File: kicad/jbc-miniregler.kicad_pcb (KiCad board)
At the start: 2 copper layers, 110 x 100 mm, 176 parts, among them J1 Makita Plus, J10 Makita Minus, J12 ActivEnergy B2-, J13 ActivEnergy B1-, J2 Makita Minus, J4 USB_B, J5 AVR ISP, J6 ActivEnergy B2+, J7 ActivEnergy B1+, J8 Makita Plus, Q1 KND3508A, Q2 2N7002, Q3 MMBT3904, Q4 MMBT3904, Q5 ZXMP10A13FTA, SW1 UP, SW2 DOWN, SW3 ENTER, SW4 BACK, SW5 Reset, SW6 Ein/Aus, U1 OLED-128x32-Module, U10 MAX3232, U11 YD3082EESA, U12 TL431, U2 74LVC1G125, U3 NST175, U4 CH340C, U5 ATmega328P-AU, U6 GS8332-SR, U7 PN7006A, U8 XL7005A, U9 XL7005A, X1 POWER, X2 COM, X3 Lötkolben, X4 GND-Öse, Y1 16MHz

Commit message: HTML-BOM aktualisiert
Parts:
- added Item5: Buchsenleiste 4P, htl_virtual:Virtual-Item, F.Cu at (141.2, 151.6)
- added R65: 56k, Resistor_SMD:R_1206_3216Metric, F.Cu at (133.1, 151.7)
- R22, R24: value 30k -> 22k
- R39: value 10k -> 22k

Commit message: Bugfix: Schottky-Diode im Schaltplan
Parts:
- added D16: SS210, htl_smd:D_SMA_wide, F.Cu at (121.0, 150.5)

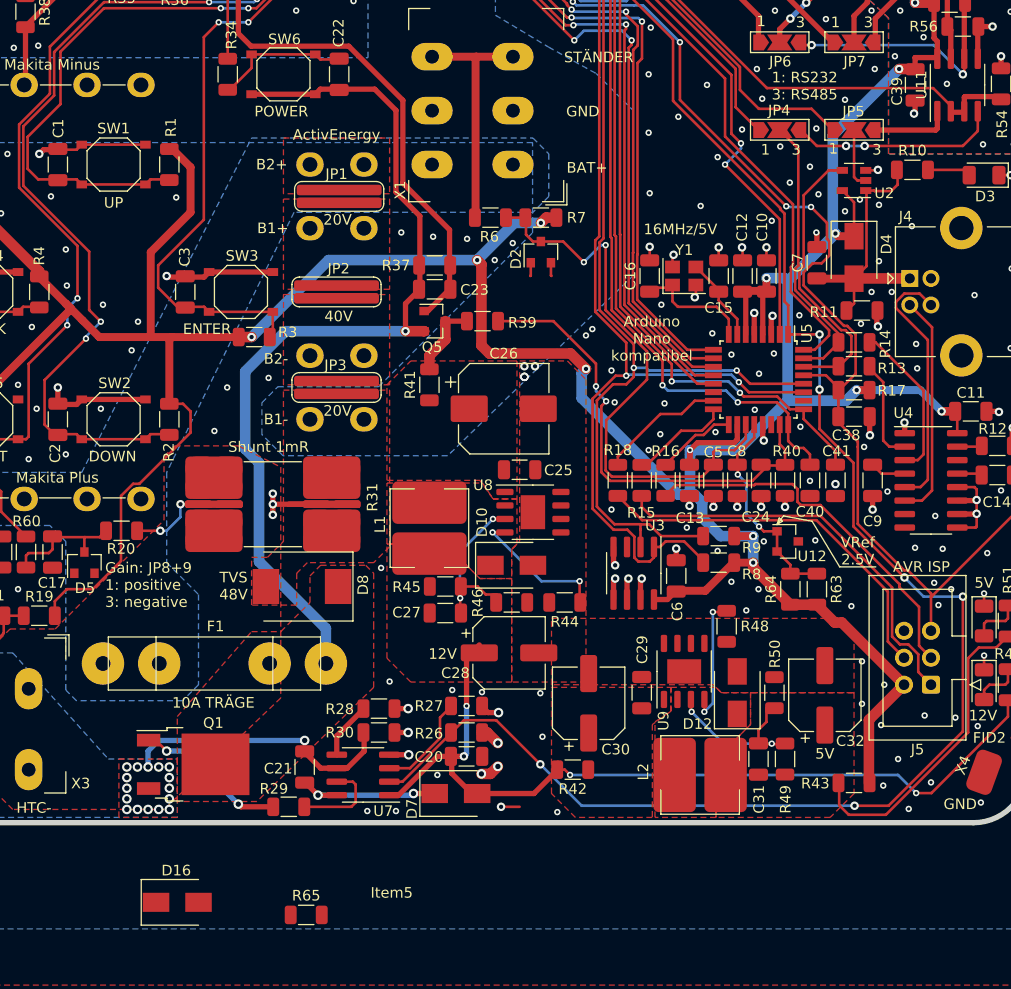
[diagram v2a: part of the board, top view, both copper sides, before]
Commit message: wip, bugfixes für v21.0.1
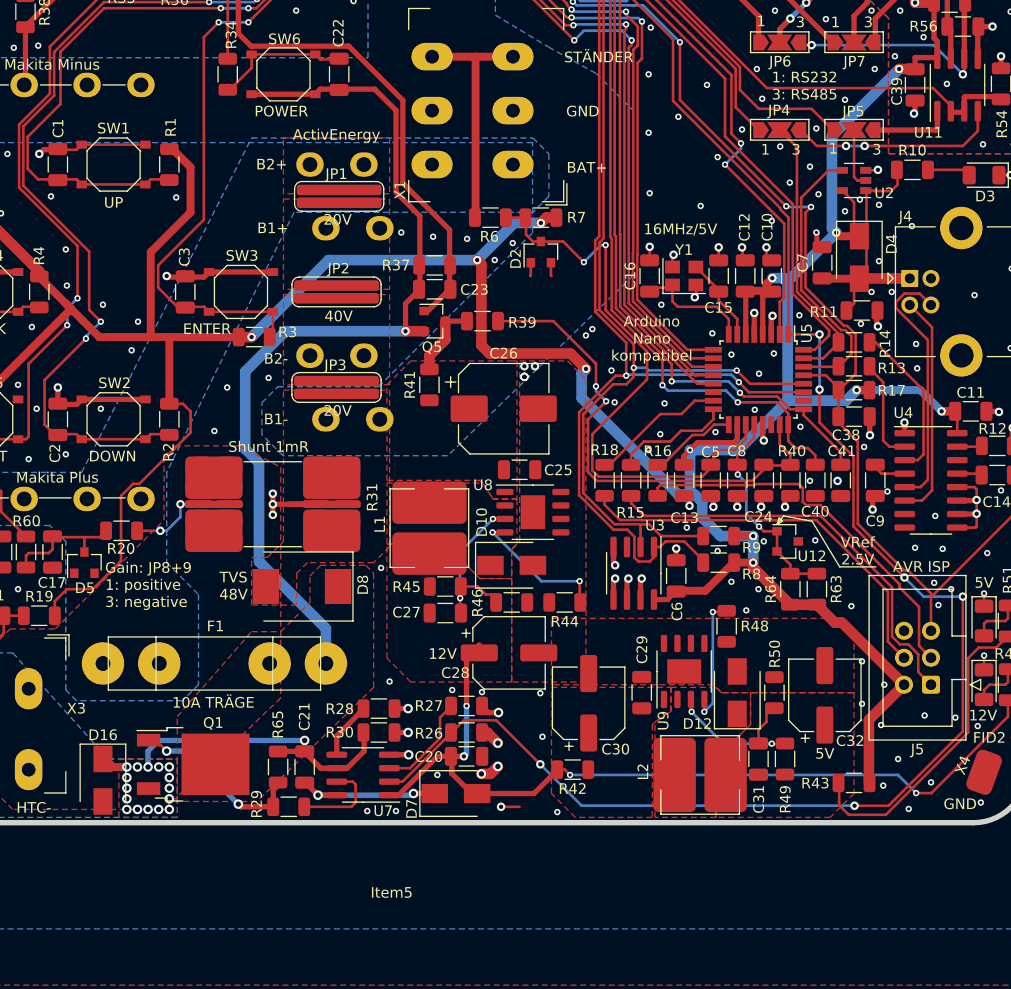
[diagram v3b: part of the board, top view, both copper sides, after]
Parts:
- moved R65 14.2 mm to (130.5, 137.8), turned to 90 degrees
- moved D16 13.5 mm to (114.0, 139.0), turned to 270 degrees
- moved J13 1.50 mm to (135.0, 105.0)
- moved J7 1.50 mm to (135.0, 87.0)
- moved R18 1.25 mm to (161.2, 110.8)
- moved R15 1.00 mm to (163.8, 110.8)
- moved R16 0.75 mm to (166.2, 110.8)
- moved C10 0.50 mm to (177.0, 91.5)
- moved C13 0.50 mm to (168.8, 110.8)
- moved C40 0.50 mm to (181.1, 110.8)
- moved C41 0.50 mm to (183.5, 110.8)
- moved C7 0.50 mm to (181.8, 90.2)
- moved D4 0.50 mm to (185.2, 89.8)
- moved R40 0.50 mm to (178.8, 110.8)
- moved C12 0.25 mm to (174.5, 91.5)
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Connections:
- D16 pad 2: GND -> /Leistungsteil/HTC-
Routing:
- net /Leistungsteil/H+: track 26.3 -> 31.1 mm
- net Net-(Q1-Pad1): track 14.4 -> 17.0 mm
- net /Stromversorgung/BattMessung: track 44.0 -> 46.5 mm
- net /Arduino/Arduino Nano/~RESET: track 204.6 -> 202.6 mm
- net Net-(J5-Pad4): track 36.0 -> 37.8 mm
- net +5V: track 446.7 -> 445.0 mm
- net /Arduino/Arduino Nano/A6: track 54.2 -> 55.8 mm
- net /Arduino/Arduino Nano/D12_MISO: track 9.48 -> 11.1 mm
- net /Arduino/Arduino Nano/D13_SCK: track 7.52 -> 8.91 mm
- net Net-(J5-Pad3): track 35.2 -> 36.5 mm
- net /Arduino/SCL: track 158.9 -> 160.0 mm
- net /Arduino/SDA: track 155.6 -> 156.7 mm
- net Net-(J5-Pad1): track 38.9 -> 39.7 mm
- net /Arduino/Arduino Nano/D11_MOSI: track 12.0 -> 12.8 mm
- net GND: vias 216 -> 215

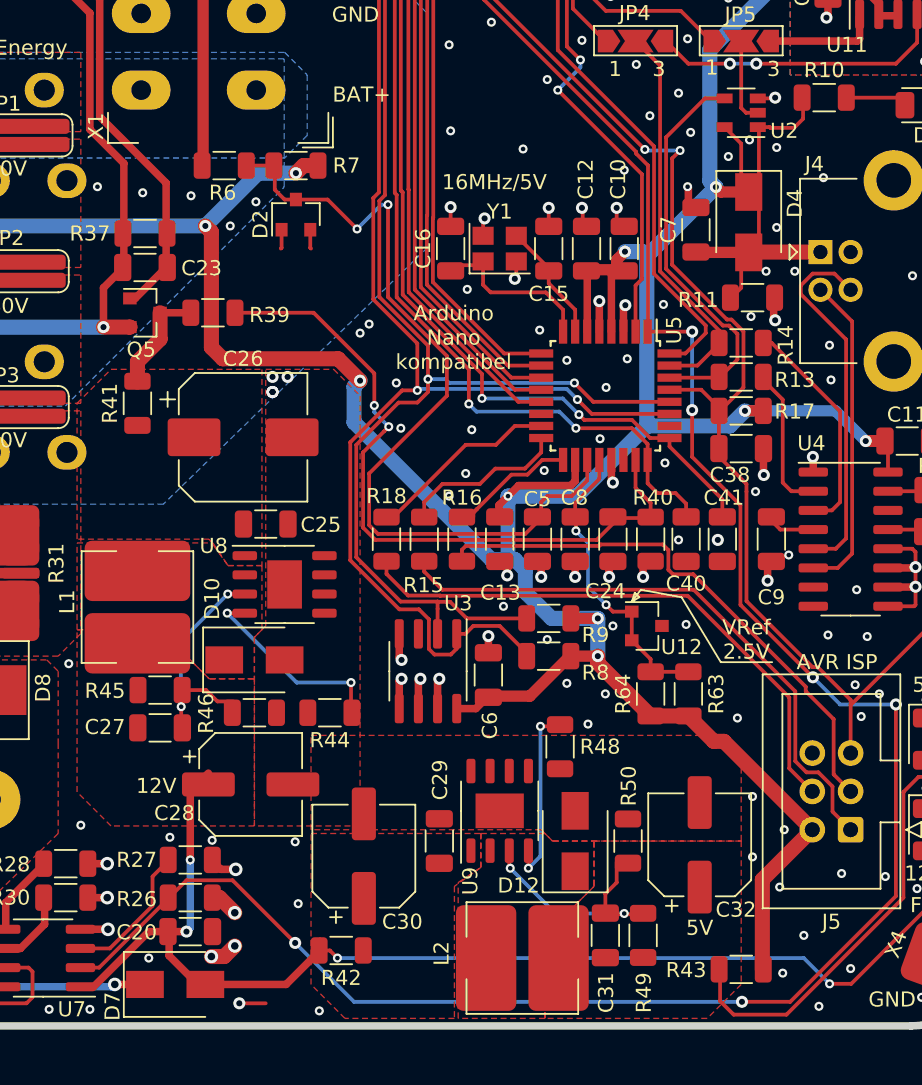
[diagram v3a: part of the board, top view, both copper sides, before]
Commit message: Workaround zu Isssue#7, USB Bootproblem
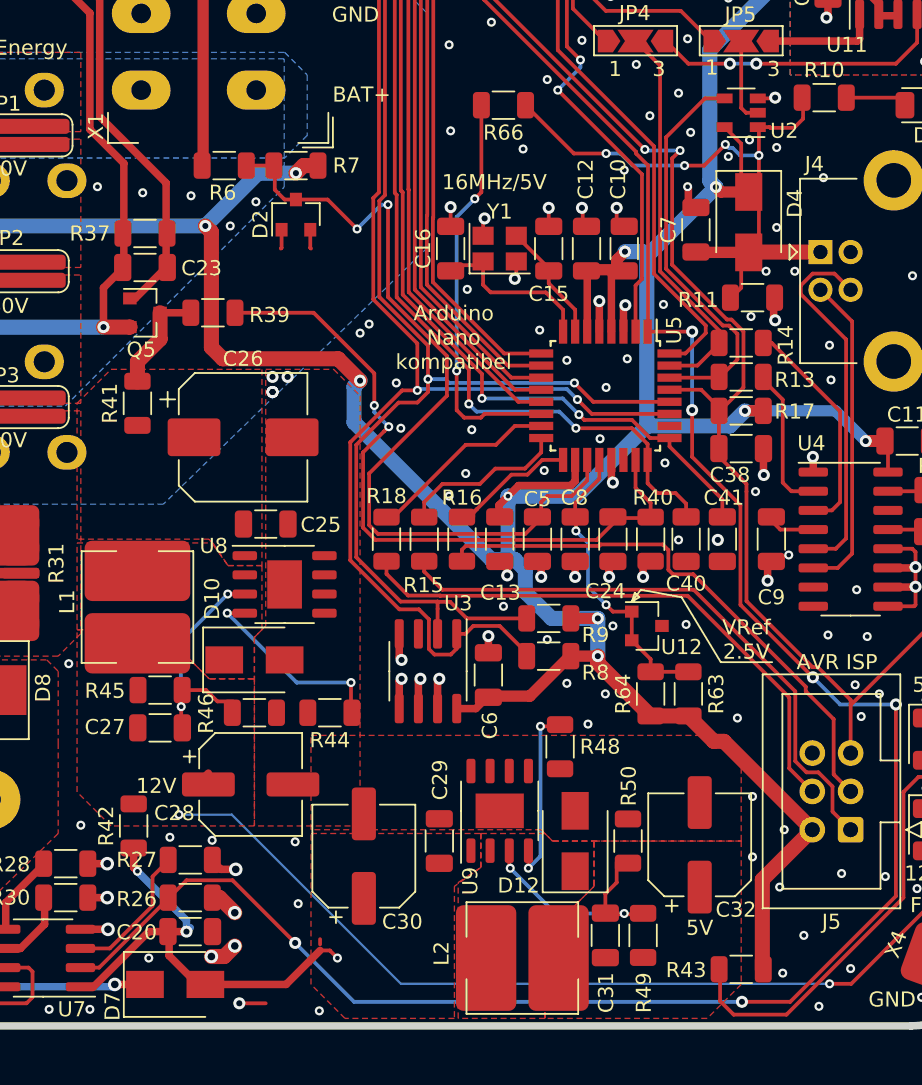
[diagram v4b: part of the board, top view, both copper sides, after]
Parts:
- added R66: 3k3, Resistor_SMD:R_1206_3216Metric, F.Cu at (169.0, 82.0)
- C10, C13, C21, C7, C8: value 1u -> 1u/100V
- moved R42 16.0 mm to (144.5, 129.8), turned to 90 degrees
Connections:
- C27 pad 1: /Leistungsteil/12V -> /Stromversorgung/12Va
- C28 pad 1: /Leistungsteil/12V -> /Stromversorgung/12Va
- C29 pad 1: /Stromversorgung/Spannungsregler 5V/IN -> /Leistungsteil/12V
- C30 pad 1: /Stromversorgung/Spannungsregler 5V/IN -> /Leistungsteil/12V
- L1 pad 2: /Leistungsteil/12V -> /Stromversorgung/12Va
- R42 pad 1: /Stromversorgung/Spannungsregler 5V/IN -> /Leistungsteil/12V
- R42 pad 2: /Leistungsteil/12V -> /Stromversorgung/12Va
- R45 pad 1: /Leistungsteil/12V -> /Stromversorgung/12Va
- R47 pad 1: /Leistungsteil/12V -> /Stromversorgung/12Va
- U5 pad 14: (no net) -> /Arduino/Arduino Nano/D10
- U9 pad 1: /Stromversorgung/Spannungsregler 5V/IN -> /Leistungsteil/12V
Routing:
- net /Stromversorgung/12Va: track 0.00 -> 62.7 mm, vias 0 -> 2
- net /Leistungsteil/12V: track 81.2 -> 30.9 mm, vias 4 -> 3
- net /Arduino/Arduino Nano/D10: track 0.00 -> 26.8 mm, vias 0 -> 2
- net /Arduino/VUSB: track 25.6 -> 43.6 mm, vias 0 -> 4
- added copper zone on F.Cu, net /Stromversorgung/12Va
- removed copper zone on F.Cu, net /Stromversorgung/Spannungsregler 5V/IN

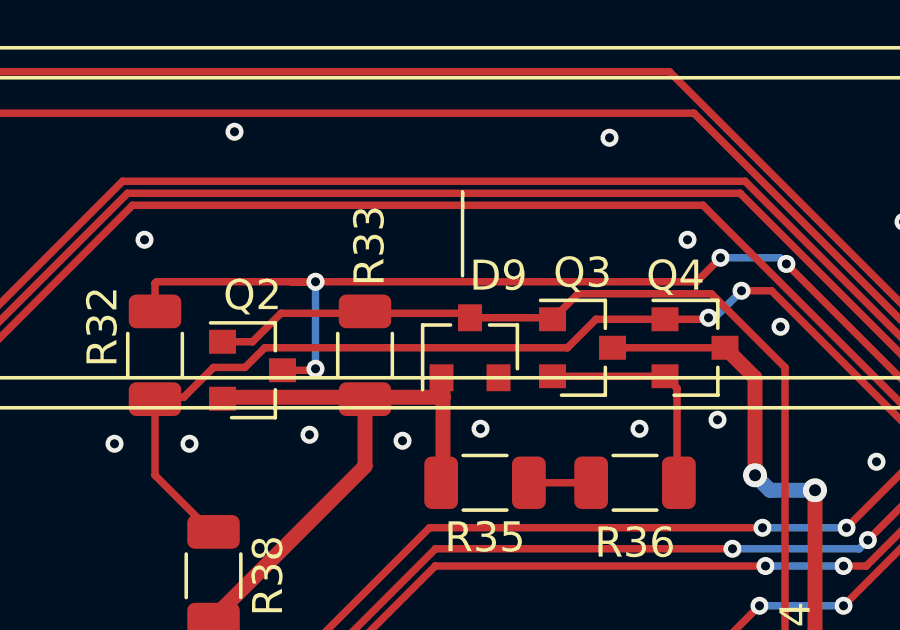
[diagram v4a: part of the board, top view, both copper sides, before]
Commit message: BOM aktualisiert, Zenerdiode: Pinout IPC-konform gestaltet, ...
siehe https://gitlab.com/kicad/libraries/kicad-symbols/-/issues/3157
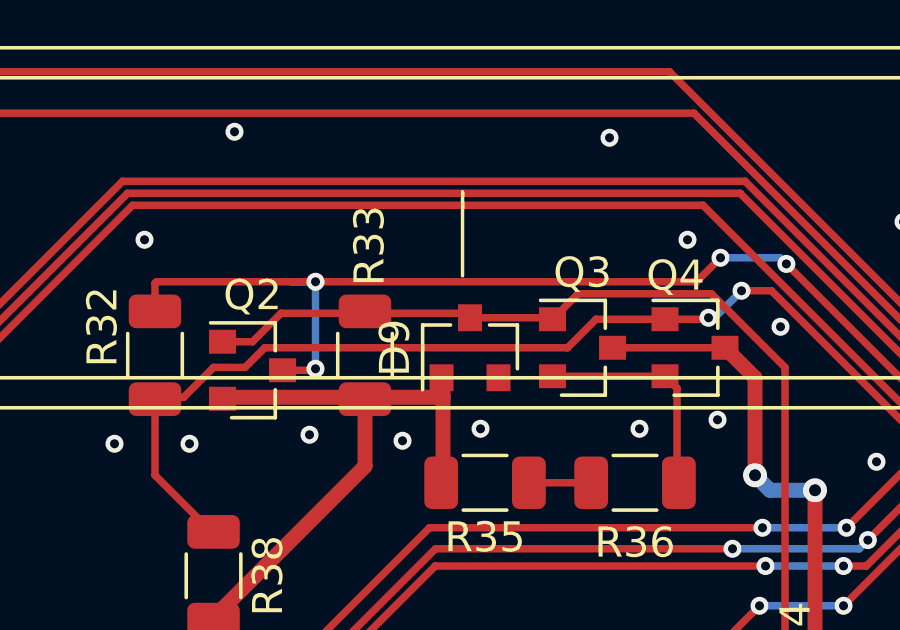
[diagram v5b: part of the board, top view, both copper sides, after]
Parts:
- D9: footprint Diode_SMD:D_SOT-23_ANK -> Package_TO_SOT_SMD:SOT-23
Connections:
- D9 pad 1: Net-(D9-Pad1) -> GNDPWR
- D9 pad 2: GNDPWR -> (no net)
- Q2 pad 1: Net-(D9-Pad1) -> Net-(D9-Pad3)
- Q3 pad 1: Net-(D9-Pad1) -> Net-(D9-Pad3)
- R33 pad 1: Net-(D9-Pad1) -> Net-(D9-Pad3)
- R34 pad 2: Net-(D9-Pad1) -> Net-(D9-Pad3)
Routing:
- net Net-(D9-Pad3): track 0.00 -> 32.0 mm
- net Net-(D9-Pad1): track 32.0 -> 0.00 mm

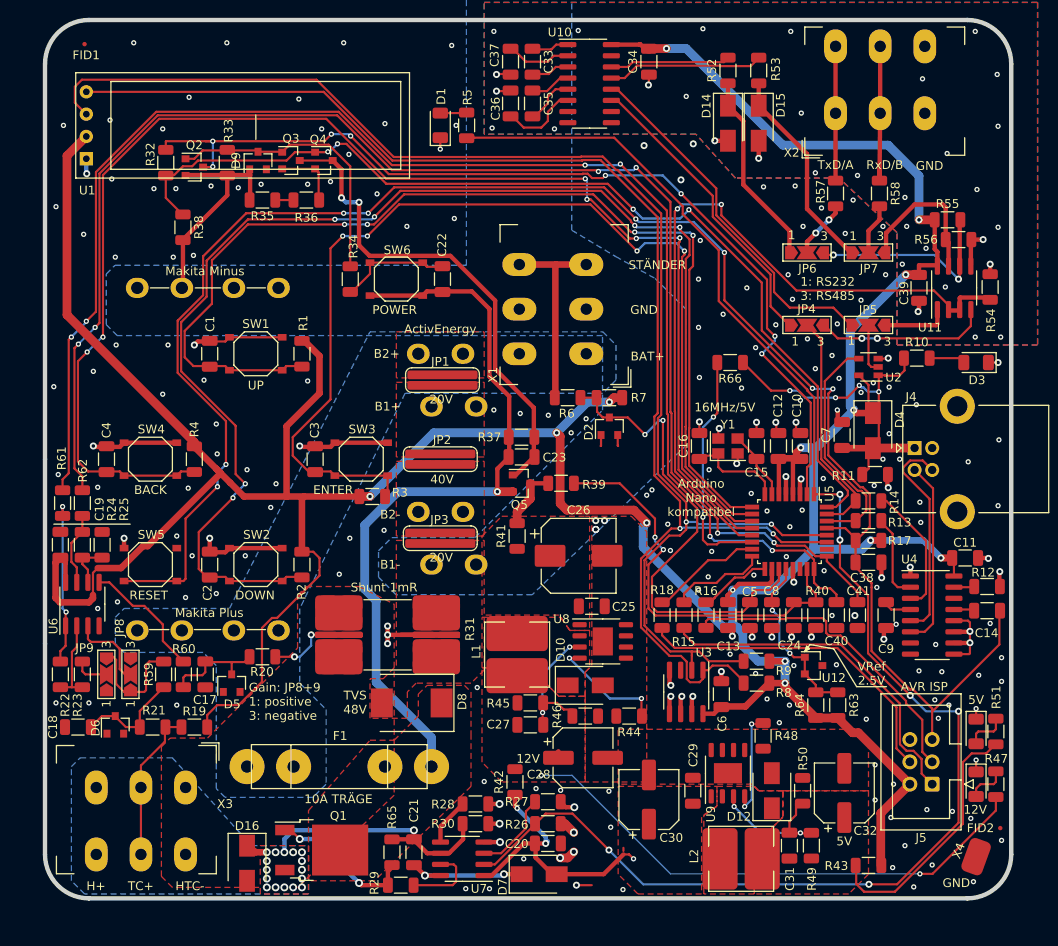
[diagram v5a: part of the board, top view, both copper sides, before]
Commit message: Überdeckende Footprints noch auseinander gerückt, ...
HTML-Bom Export und Gerber-Export, 40 Stück bestell bei MulitCB
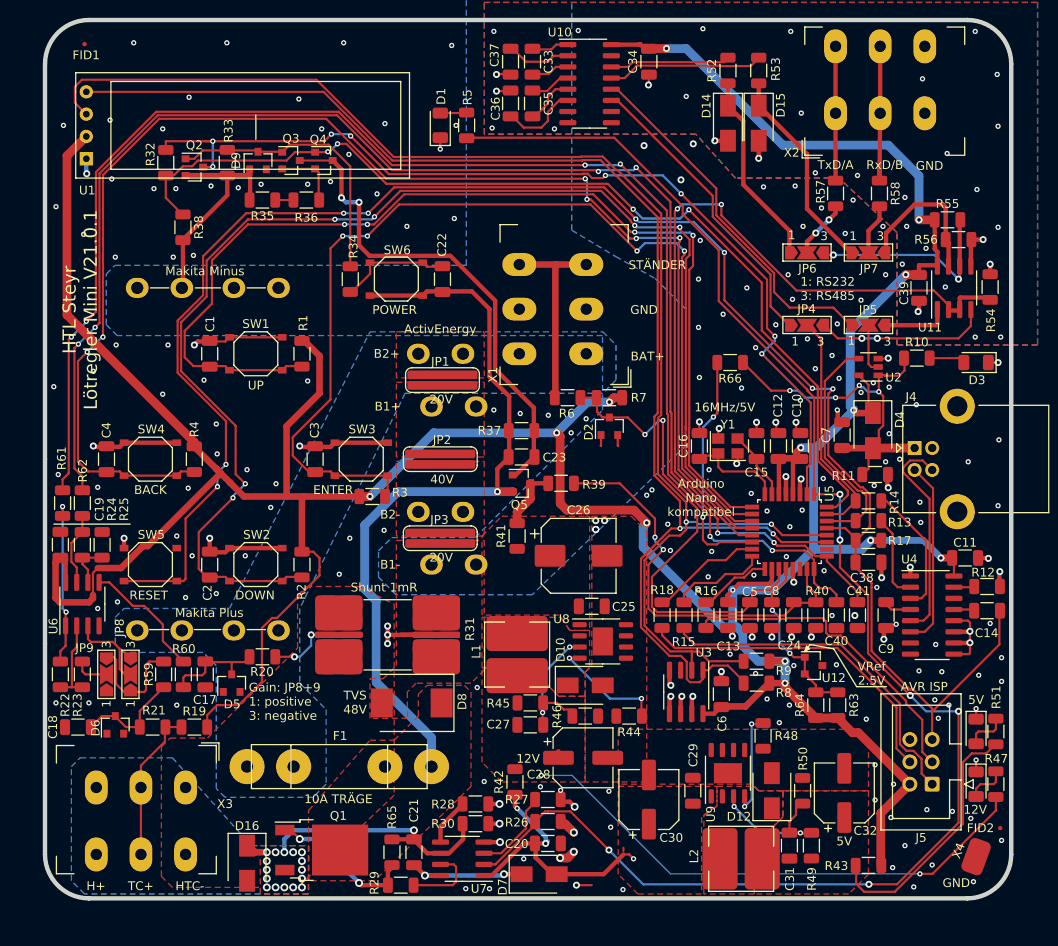
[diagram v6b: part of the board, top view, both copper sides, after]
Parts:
- moved R37 0.75 mm to (145.2, 89.8)
- moved R26 0.25 mm to (148.2, 134.2)
- moved R27 0.25 mm to (148.2, 131.8)
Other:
- board text added: "HTL Steyr Lötregler Mini V21.0.1"
- board text removed: "HTL Steyr Lötregler Mini V21.0.0"
